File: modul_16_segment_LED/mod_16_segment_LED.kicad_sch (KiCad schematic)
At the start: 28 parts

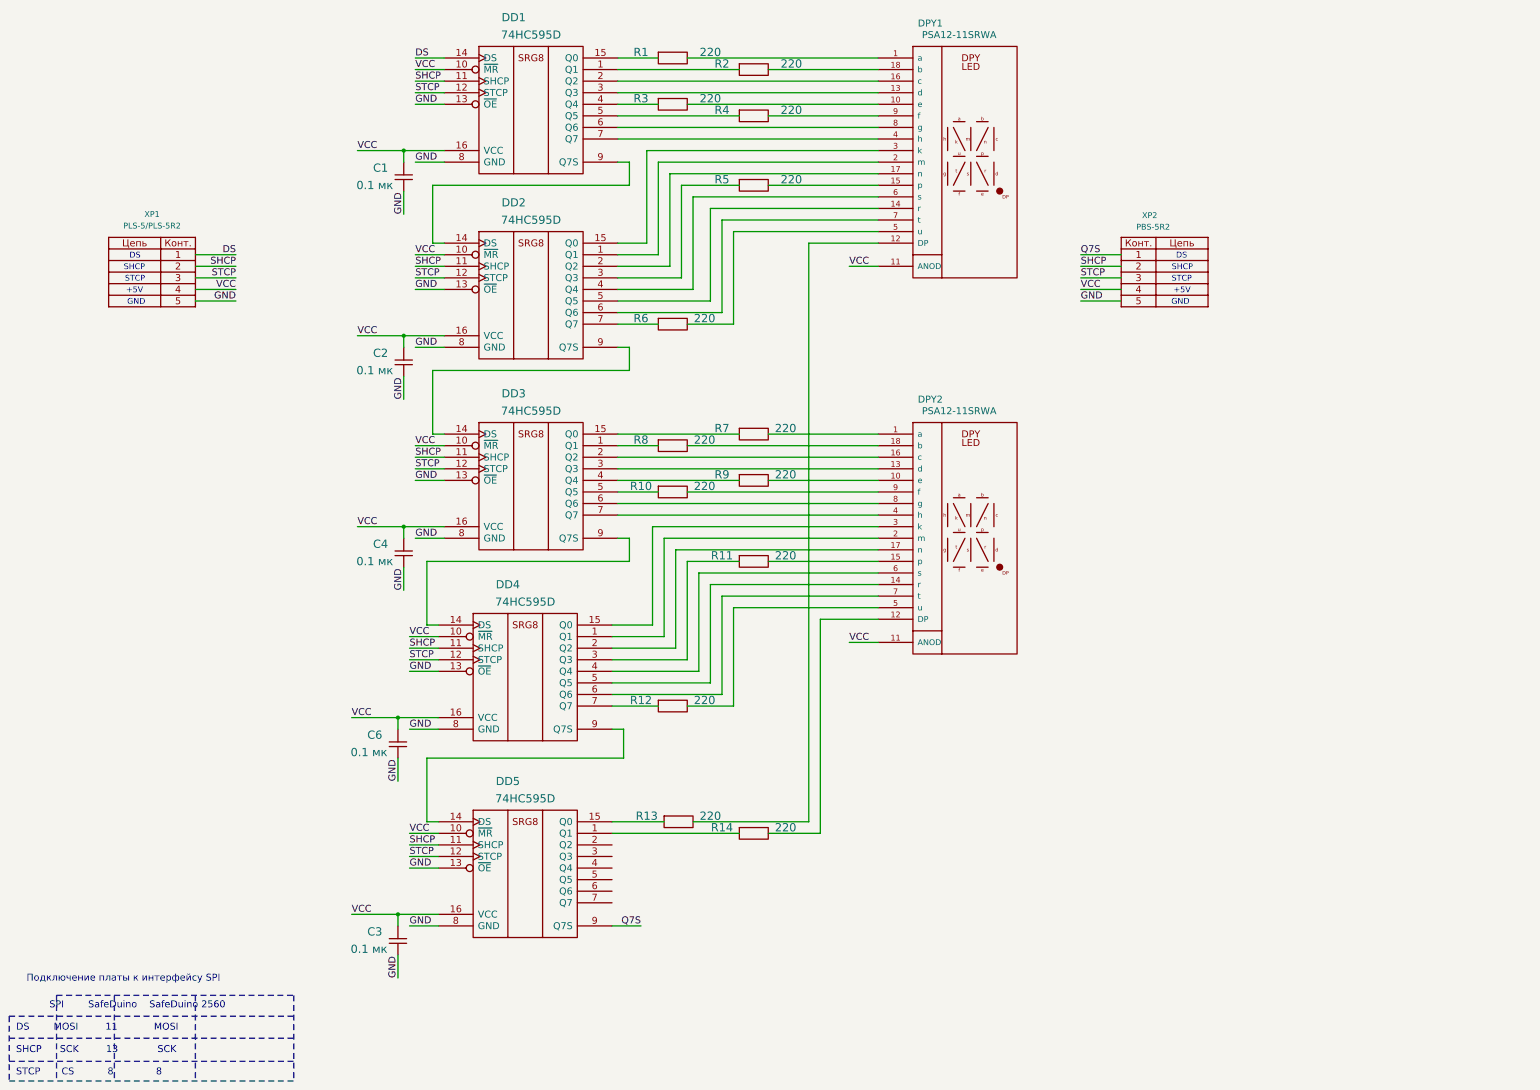
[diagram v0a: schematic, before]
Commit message: Добавил дополнительные резисторы в схему16-ти сегментного индикатора.
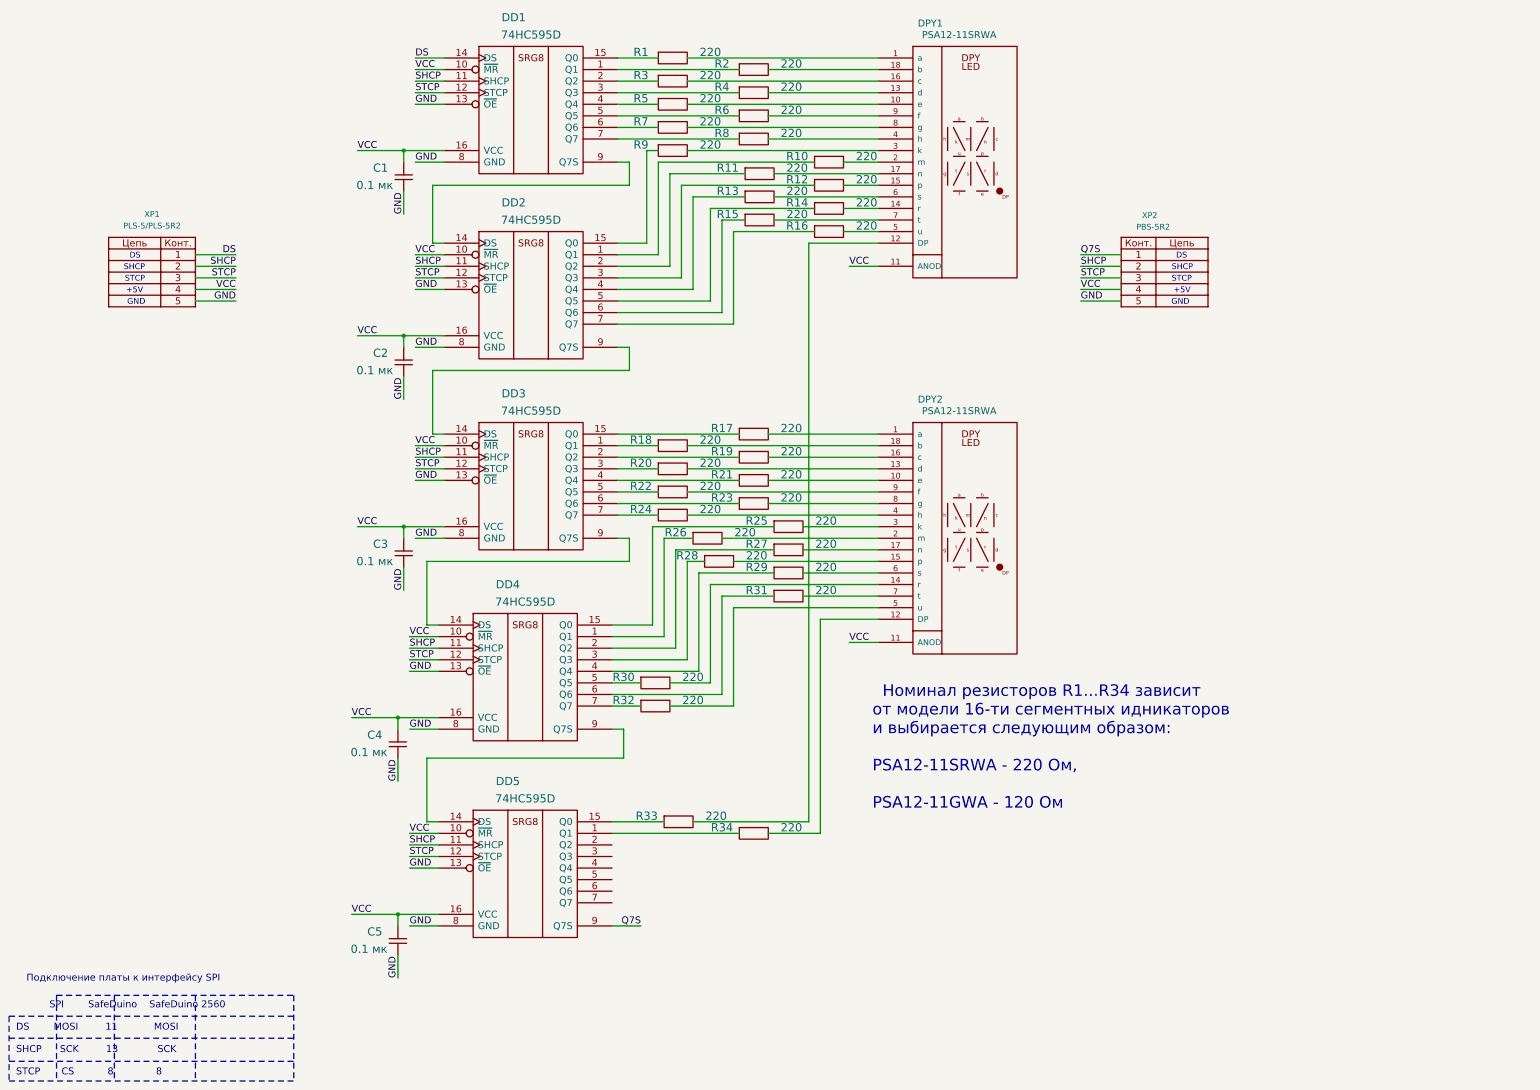
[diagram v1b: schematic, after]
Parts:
- added R15, R16, R17, R18, R19, R20, R21, R22, R23, R24, R25, R26, R27, R28, R29, R30, R31, R32, R33, R34: 220, IWsmd_case:SMD0805, symbol mod_16_segment_LED-rescue:RESISTOR
- C1, C2, C3, C4, R1, R10, R11, R12, R13, R14, R2, R3, R4, R5, R6, R7, R8, R9: footprint (none) -> IWsmd_case:SMD0805
- C5: renamed from C6; footprint (none) -> IWsmd_case:SMD0805
- DD1, DD2, DD3, DD4, DD5: footprint (none) -> IWsmd_case:SOIC16
- DPY1, DPY2: footprint (none) -> IWcomponents:PSA12-11
- XP1, XP2: footprint (none) -> IWconnectors:PIN_ARRAY_5x1
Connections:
- net at DD1.2 (Q2): now also R3.1; no longer DPY1.16 (c)
- net at DD1.3 (Q3): now also R4.1; no longer DPY1.13 (d)
- net at DD1.4 (Q4): now also R5.1; no longer R3.1
- net at DD1.5 (Q5): now also R6.1; no longer R4.1
- net at DD1.6 (Q6): now also R7.1; no longer DPY1.8 (g)
- net at DD1.7 (Q7): now also R8.1; no longer DPY1.4 (h)
- net at DD2.1 (Q1): now also R10.1; no longer DPY1.2 (m)
- net at DD2.15 (Q0): now also R9.1; no longer DPY1.3 (k)
- net at DD2.2 (Q2): now also R11.1; no longer DPY1.17 (n)
- net at DD2.3 (Q3): now also R12.1; no longer R5.1
- net at DD2.4 (Q4): now also R13.1; no longer DPY1.6 (s)
- net at DD2.5 (Q5): now also R14.1; no longer DPY1.14 (r)
- net at DD2.6 (Q6): now also R15.1; no longer DPY1.7 (t)
- net at DD2.7 (Q7): now also R16.1; no longer R6.1
- net at DPY1.10 (e): now also R5.2; no longer R3.2
- net at DPY1.12 (DP): now also R33.2; no longer R13.2
- net at DPY1.15 (p): now also R12.2; no longer R5.2
- net at DPY1.5 (u): now also R16.2; no longer R6.2
- net at R4.2: now also DPY1.13 (d); no longer DPY1.9 (f)
- net at DD3.1 (Q1): now also R18.1; no longer R8.1
- net at DD3.15 (Q0): now also R17.1; no longer R7.1
- net at DD3.2 (Q2): now also R19.1; no longer DPY2.16 (c)
- net at DD3.3 (Q3): now also R20.1; no longer DPY2.13 (d)
- net at DD3.4 (Q4): now also R21.1; no longer R9.1
- net at DD3.5 (Q5): now also R22.1; no longer R10.1
- net at DD3.6 (Q6): now also R23.1; no longer DPY2.8 (g)
- net at DD3.7 (Q7): now also R24.1; no longer DPY2.4 (h)
- net at DD5.1 (Q1): now also R34.1; no longer R14.1
- net at R14.2: now also DPY1.14 (r); no longer DPY2.12 (DP)
- net at R7.2: now also DPY1.8 (g); no longer DPY2.1 (a)
- net at R9.2: now also DPY1.3 (k); no longer DPY2.10 (e)
- net at DPY2.14 (r): now also R30.2; no longer DD4.5 (Q5)
- net at R11.2: now also DPY1.17 (n); no longer DPY2.15 (p)
- net at DPY2.17 (n): now also R27.2; no longer DD4.2 (Q2)
- net at R8.2: now also DPY1.4 (h); no longer DPY2.18 (b)
- net at DPY2.2 (m): now also R26.2; no longer DD4.1 (Q1)
- net at DPY2.3 (k): now also R25.2; no longer DD4.15 (Q0)
- net at DPY2.5 (u): now also R32.2; no longer R12.2
- net at DPY2.6 (s): now also R29.2; no longer DD4.4 (Q4)
- net at DPY2.7 (t): now also R31.2; no longer DD4.6 (Q6)
- net at R10.2: now also DPY1.2 (m); no longer DPY2.9 (f)
- net at DD4.3 (Q3): now also R28.1; no longer R11.1
- net at DD4.7 (Q7): now also R32.1; no longer R12.1
- net at DD5.15 (Q0): now also R33.1; no longer R13.1
- new net: DPY1.16 (c), R3.2
- new net: DPY1.6 (s), R13.2
- new net: DPY1.7 (t), R15.2
- new net: DPY1.9 (f), R6.2
- new net: DPY2.1 (a), R17.2
- new net: DPY2.10 (e), R21.2
- new net: DPY2.12 (DP), R34.2
- new net: DPY2.13 (d), R20.2
- new net: DPY2.15 (p), R28.2
- new net: DPY2.16 (c), R19.2
- new net: DPY2.18 (b), R18.2
- new net: DPY2.4 (h), R24.2
- new net: DPY2.8 (g), R23.2
- new net: DPY2.9 (f), R22.2
- new net: DD4.1 (Q1), R26.1
- new net: DD4.15 (Q0), R25.1
- new net: DD4.2 (Q2), R27.1
- new net: DD4.4 (Q4), R29.1
- new net: DD4.5 (Q5), R30.1
- new net: DD4.6 (Q6), R31.1
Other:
- note added: "Номинал резисторов R1...R34 зависит от модели 16-ти сегментных идникаторов и выбирается следующим образом: PSA12-11SRWA - 220 Ом, PSA12-11GWA - 120 Ом"
- moved on the sheet: C3, C4, C5
